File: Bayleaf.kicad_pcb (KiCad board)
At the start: 2 copper layers, 276 x 94 mm, 148 parts

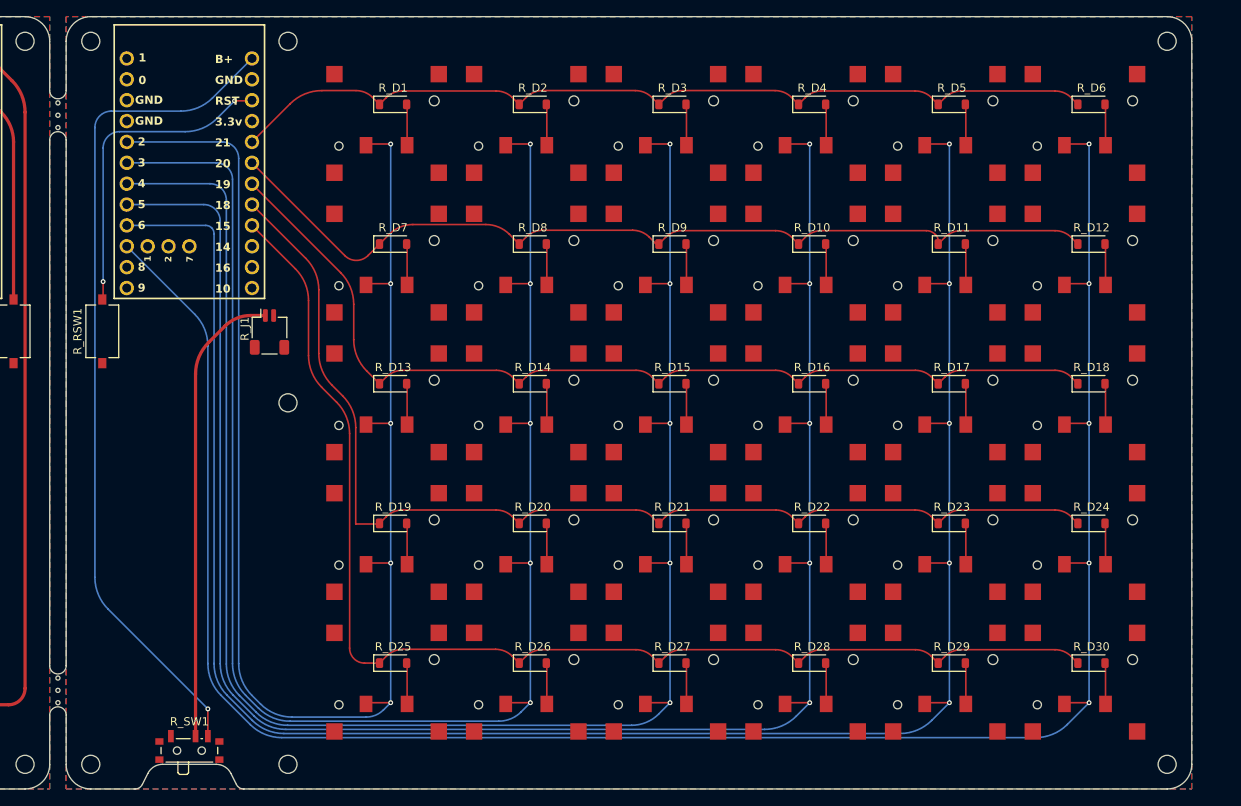
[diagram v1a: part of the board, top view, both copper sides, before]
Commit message: fix v-scoring
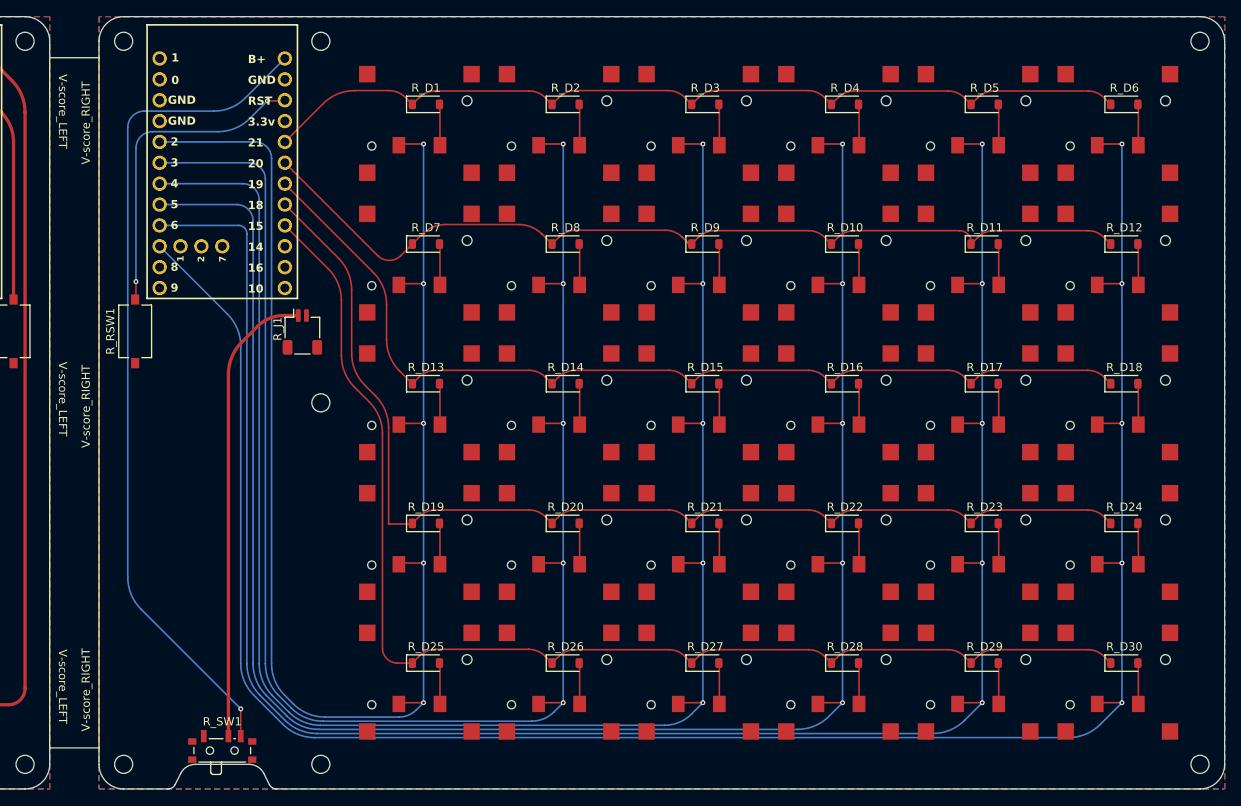
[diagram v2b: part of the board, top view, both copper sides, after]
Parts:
- removed ? (x6): , 
- moved R_D1 4.00 mm to (182.8, 10.7)
- moved R_D10 4.00 mm to (233.8, 27.7)
- moved R_D11 4.00 mm to (250.8, 27.7)
- moved R_D12 4.00 mm to (267.8, 27.7)
- moved R_D13 4.00 mm to (182.8, 44.7)
- moved R_D14 4.00 mm to (199.8, 44.7)
- moved R_D15 4.00 mm to (216.8, 44.7)
- moved R_D16 4.00 mm to (233.8, 44.7)
- moved R_D17 4.00 mm to (250.8, 44.7)
- moved R_D18 4.00 mm to (267.8, 44.7)
- moved R_D19 4.00 mm to (182.8, 61.7)
- moved R_D2 4.00 mm to (199.8, 10.7)
- moved R_D20 4.00 mm to (199.8, 61.7)
- moved R_D21 4.00 mm to (216.8, 61.7)
- moved R_D22 4.00 mm to (233.8, 61.7)
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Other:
- board size 276 x 94 mm -> 280 x 94 mm
- board text added: "V-score_LEFT"
- board text added: "V-score_RIGHT"

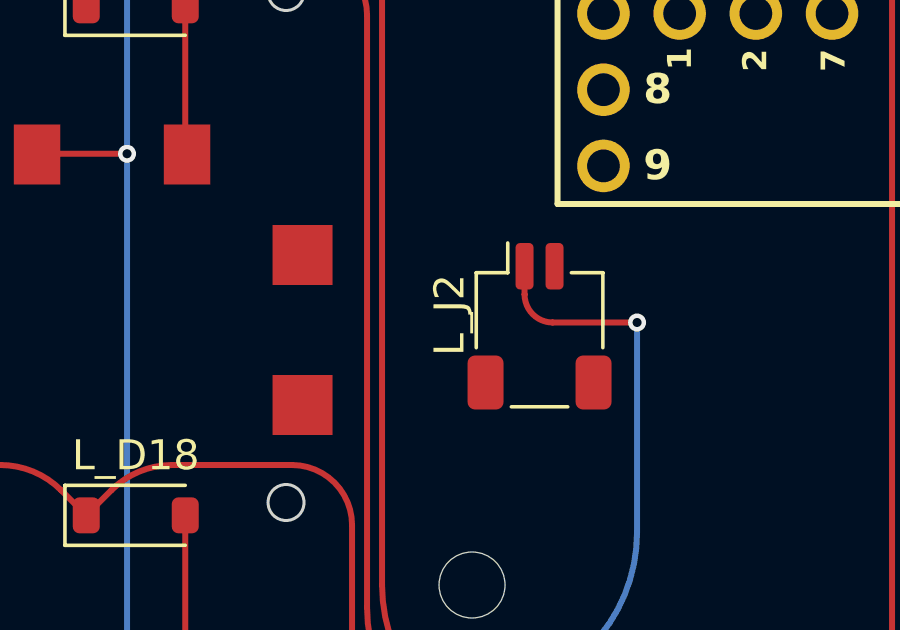
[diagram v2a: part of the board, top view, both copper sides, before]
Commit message: fix v-score + edge zone fill fix
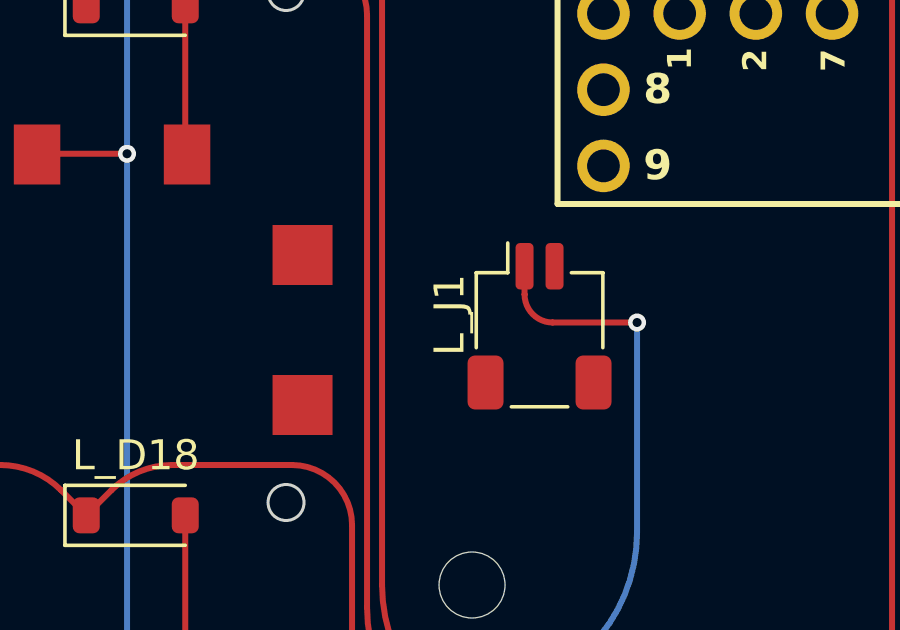
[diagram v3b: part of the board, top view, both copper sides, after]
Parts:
- renumbered L_J2 to L_J1
